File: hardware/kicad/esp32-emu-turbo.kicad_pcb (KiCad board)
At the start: 4 copper layers, 160 x 75 mm, 89 parts, among them J1 USB-C-16P, J3 JST-PH-2P-SMD, J4 FPC-40P-0.5mm, SW1 SW-SMD-5.1x5.1, SW10 SW-SMD-5.1x5.1, SW11 SW-SMD-5.1x5.1, SW12 SW-SMD-5.1x5.1, SW13 SW-SMD-5.1x5.1, SW2 SW-SMD-5.1x5.1, SW3 SW-SMD-5.1x5.1, SW4 SW-SMD-5.1x5.1, SW5 SW-SMD-5.1x5.1, SW6 SW-SMD-5.1x5.1, SW7 SW-SMD-5.1x5.1, SW8 SW-SMD-5.1x5.1, SW9 SW-SMD-5.1x5.1, U1 ESP32-S3-WROOM-1-N16R8, U2 ESOP-8, U3 SOT-223, U4 SOT-23-6, U5 SOP-16, U6 TF-01A

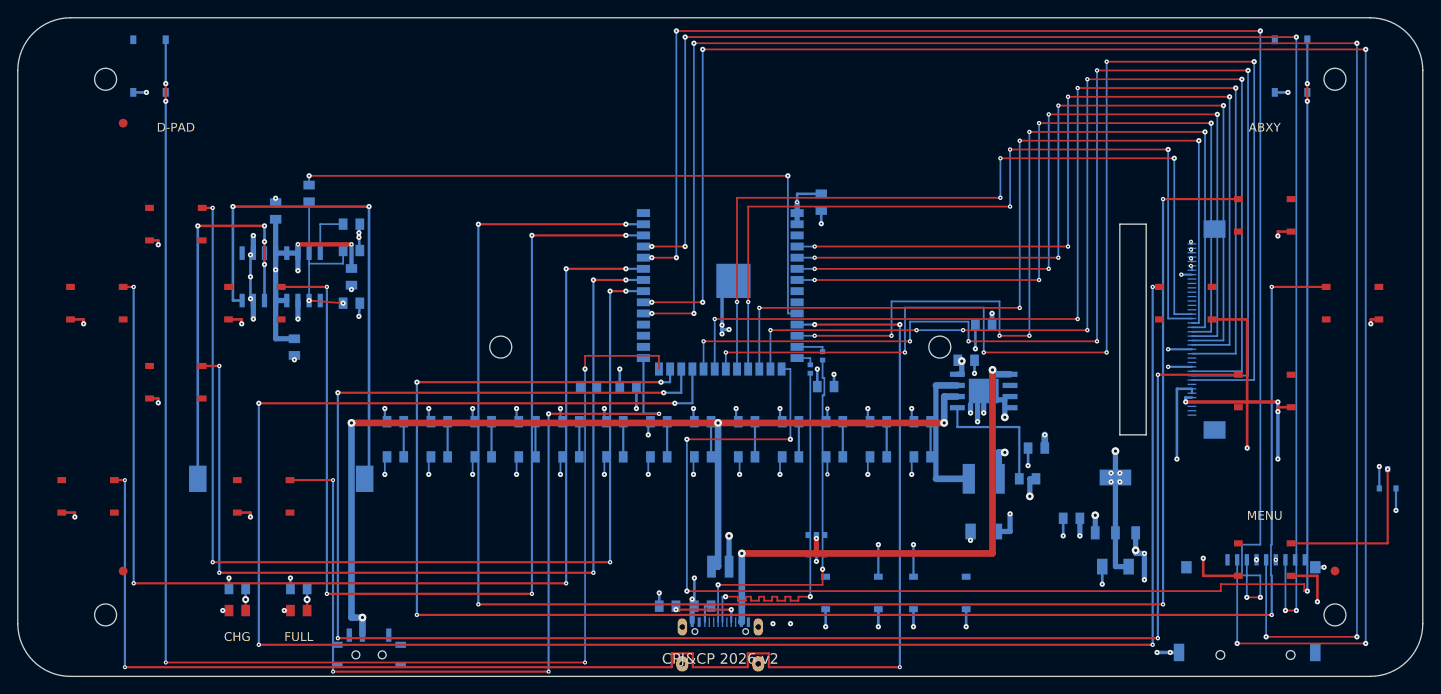
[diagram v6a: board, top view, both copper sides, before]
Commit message: fix(dfm): resolve 4 trace/via clearance violations + fix via-to-SMD false positive
- BTN_L approach column: shift x=64.60→64.75 (R8/C9 pad gap 0.05→0.20mm)
- BTN_UP approach column: add post-allocation pad clearance enforcement
  with oscillation-aware iteration (escapes R9/C10 pad cluster)
- BAT+ via: shift x=79.95→80.02 (R11 ring-to-pad gap 0.05→0.12mm)
- verify_dfm_v2.py: fix via-to-SMD test — use rectangular pad proximity
  instead of circumscribed circle (was inflating 1.0x1.3mm pad to r=0.82mm)
- New skill: /pcb-to-firmware (auto-propagate PCB changes to firmware)
- Updated PCBA renders (11 views, 1920x1080 raytraced)

Results: 115 DFM passed, 0 failed | 9 DFA passed | 358 design intent passed

Co-Authored-By: Claude Opus 4.6 (1M context) <noreply@anthropic.com>
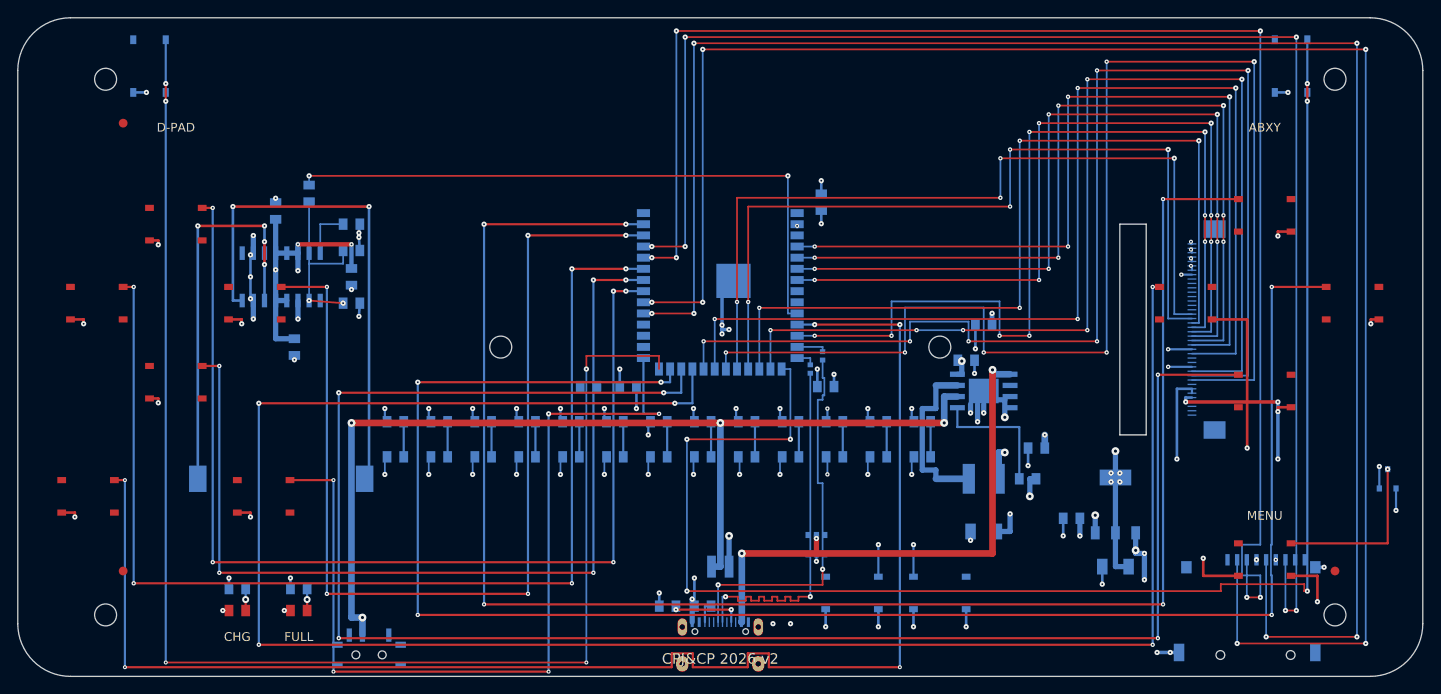
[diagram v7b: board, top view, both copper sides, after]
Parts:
- removed the C3 at (69.5, 42.0)
- removed the C4 at (92.0, 42.0)
- removed the C6 at (48.0, 50.0)
- removed the J1 at (80.0, 71.2)
- removed the J3 at (80.0, 62.5)
- removed the L1 at (110.0, 52.5)
- removed the R13 at (88.0, 46.0)
- removed the R14 at (93.0, 46.0)
- removed the R15 at (98.0, 46.0)
- removed the R16 at (115.0, 52.5)
- removed the R17 at (25.0, 65.0)
- removed the R18 at (32.0, 65.0)
- removed the R19 at (103.0, 46.0)
- removed the R22 at (90.2, 40.0)
- removed the R23 at (91.7, 38.5)
- removed the R3 at (65.0, 42.0)
- removed the R4 at (43.0, 46.0)
- removed the R5 at (48.0, 46.0)
- removed the R6 at (53.0, 46.0)
- removed the R7 at (58.0, 46.0)
- removed the R8 at (63.0, 46.0)
- removed the R9 at (68.0, 46.0)
- removed the SW5 at (142.0, 22.5)
- removed the SW6 at (152.0, 32.5)
- removed the SW7 at (142.0, 42.5)
- removed the U2 at (110.0, 42.5)
- removed the U4 at (91.0, 60.0)
- removed the U5 at (30.0, 29.5)
- added C1: C_0805, C_0805, B.Cu at (120.0, 57.0)
- added C10: C_0805, C_0805, B.Cu at (68.0, 50.0)
- added C11: C_0805, C_0805, B.Cu at (73.0, 50.0)
- added C12: C_0805, C_0805, B.Cu at (78.0, 50.0)
- added C13: C_0805, C_0805, B.Cu at (83.0, 50.0)
- added C14: C_0805, C_0805, B.Cu at (88.0, 50.0)
- added C15: C_0805, C_0805, B.Cu at (93.0, 50.0)
- added C16: C_0805, C_0805, B.Cu at (98.0, 50.0)
- added C17: C_0805, C_0805, B.Cu at (110.0, 35.0)
- added C18: C_0805, C_0805, B.Cu at (116.0, 49.0)
- added C19: C_1206, C_1206, B.Cu at (110.0, 58.5)
- added C2: C_1206, C_1206, B.Cu at (125.0, 62.5)
- added C20: C_0805, C_0805, B.Cu at (103.0, 50.0)
- added C21: C_0805, C_0805, B.Cu at (38.0, 23.5)
- added C22: C_0805, C_0805, B.Cu at (33.2, 20.0)
- added C23: C_0805, C_0805, B.Cu at (38.0, 29.5)
- added C24: C_0805, C_0805, B.Cu at (29.4, 22.0)
- added C25: C_0805, C_0805, B.Cu at (31.5, 37.5)
- added C27: C_0805, C_0805, B.Cu at (108.0, 39.0)
- added C8: C_0805, C_0805, B.Cu at (58.0, 50.0)
- added C9: C_0805, C_0805, B.Cu at (63.0, 50.0)
- added FID3: Fiducial, Fiducial, F.Cu at (12.0, 63.0)
- added R20: R_0805, R_0805, B.Cu at (38.0, 26.5)
- added R21: R_0805, R_0805, B.Cu at (38.0, 32.5)
- added SW11: SW-SMD-5.1x5.1, SW-SMD-5.1x5.1, B.Cu at (15.0, 5.50)
- added SW_RST: SW-SMD-5.1x5.1, SW-SMD-5.1x5.1, B.Cu at (95.0, 65.5)
- added U1: ESP32-S3-WROOM-1-N16R8, ESP32-S3-WROOM-1-N16R8, B.Cu at (80.0, 27.5)
- added U6: TF-01A, TF-01A, B.Cu at (140.0, 67.0)
- C6: renamed from FID3; value Fiducial -> C_0805; footprint Fiducial -> C_0805; moved to B.Cu
- J1: renamed from SW_RST; value SW-SMD-5.1x5.1 -> USB-C-16P; footprint SW-SMD-5.1x5.1 -> USB-C-16P
- J3: renamed from R12; value R_0805 -> JST-PH-2P-SMD; footprint R_0805 -> JST-PH-2P-SMD
- L1: renamed from R11; value R_0805 -> SMD-4x4x2; footprint R_0805 -> SMD-4x4x2
- R12: renamed from C21; value C_0805 -> R_0805; footprint C_0805 -> R_0805
- R13: renamed from C23; value C_0805 -> R_0805; footprint C_0805 -> R_0805
- R14: renamed from C24; value C_0805 -> R_0805; footprint C_0805 -> R_0805
- R15: renamed from C25; value C_0805 -> R_0805; footprint C_0805 -> R_0805
- R16: renamed from C2; value C_1206 -> R_0805; footprint C_1206 -> R_0805
- R17: renamed from C15; value C_0805 -> R_0805; footprint C_0805 -> R_0805
- R18: renamed from C16; value C_0805 -> R_0805; footprint C_0805 -> R_0805
- R19: renamed from C1; value C_0805 -> R_0805; footprint C_0805 -> R_0805
- R22: renamed from C9; value C_0805 -> R_0402; footprint C_0805 -> R_0402
- R23: renamed from C10; value C_0805 -> R_0402; footprint C_0805 -> R_0402
- R3: renamed from C11; value C_0805 -> R_0805; footprint C_0805 -> R_0805
- R4: renamed from C20; value C_0805 -> R_0805; footprint C_0805 -> R_0805
- R5: renamed from C17; value C_0805 -> R_0805; footprint C_0805 -> R_0805
- R6: renamed from C18; value C_0805 -> R_0805; footprint C_0805 -> R_0805
- R7: renamed from C19; value C_1206 -> R_0805; footprint C_1206 -> R_0805
- R8: renamed from C27; value C_0805 -> R_0805; footprint C_0805 -> R_0805
- R9: renamed from C22; value C_0805 -> R_0805; footprint C_0805 -> R_0805
- SW12: renamed from U6; value TF-01A -> SW-SMD-5.1x5.1; footprint TF-01A -> SW-SMD-5.1x5.1
- SW5: renamed from U1; value ESP32-S3-WROOM-1-N16R8 -> SW-SMD-5.1x5.1; footprint ESP32-S3-WROOM-1-N16R8 -> SW-SMD-5.1x5.1; moved to F.Cu
- SW6: renamed from SW11; moved to F.Cu
- SW7: renamed from SW12; moved to F.Cu
- U2: renamed from C26; value C_0805 -> ESOP-8; footprint C_0805 -> ESOP-8
- U4: renamed from C8; value C_0805 -> SOT-23-6; footprint C_0805 -> SOT-23-6
- U5: renamed from R10; value R_0805 -> SOP-16; footprint R_0805 -> SOP-16
- moved SW6 139.6 mm to (152.0, 32.5)
- moved R17 69.6 mm to (25.0, 65.0)
- moved R14 68.0 mm to (93.0, 46.0)
- moved R18 67.7 mm to (32.0, 65.0)
- moved R15 67.0 mm to (98.0, 46.0)
- moved R6 63.1 mm to (53.0, 46.0)
- moved R5 63.0 mm to (48.0, 46.0)
- moved SW5 62.2 mm to (142.0, 22.5)
- moved SW12 61.7 mm to (145.0, 5.50)
- moved R4 60.1 mm to (43.0, 46.0)
- moved R7 53.5 mm to (58.0, 46.0)
- moved R13 52.7 mm to (88.0, 46.0)
- moved R12 50.3 mm to (83.0, 46.0)
- moved U5 46.1 mm to (30.0, 29.5)
- moved R8 45.5 mm to (63.0, 46.0)
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- renumbered C14 to C26, C12 to C3, C13 to C4, R20 to R10, R21 to R11
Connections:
- C26 pad 1: (no net) -> +3V3
- C26 pad 2: (no net) -> GND
- C3 pad 1: (no net) -> +3V3
- C3 pad 2: (no net) -> GND
- C4 pad 1: (no net) -> +3V3
- C4 pad 2: (no net) -> GND
- C5 pad 1: (no net) -> BTN_UP
- C5 pad 2: (no net) -> GND
- C6 pad 1: (no net) -> BTN_DOWN
- C7 pad 1: (no net) -> BTN_LEFT
- C7 pad 2: (no net) -> GND
- J1 pad 1: EN -> GND
- J1 pad 2: (no net) -> VBUS
- J1 pad 3: GND -> (no net)
- J1 pad 4: GND -> USB_CC1
- J3 pad 1: (no net) -> BAT+
- J3 pad 2: (no net) -> GND
- J4 pad 37: (no net) -> GND
- L1 pad 1: (no net) -> BAT+
- L1 pad 2: (no net) -> LX
- R10 pad 1: GND -> BTN_X
- R10 pad 2: I2S_DOUT -> +3V3
- R11 pad 1: GND -> BTN_Y
- R11 pad 2: I2S_DOUT -> +3V3
- R12 pad 1: GND -> BTN_START
- R12 pad 2: PAM_VREF -> +3V3
- R13 pad 1: +5V -> BTN_SELECT
- R13 pad 2: GND -> +3V3
- R14 pad 1: GND -> BTN_L
- R14 pad 2: +5V -> +3V3
- R15 pad 1: +5V -> BTN_R
- R15 pad 2: GND -> +3V3
- R16 pad 1: +3V3 -> +5V
- R16 pad 2: GND -> IP5306_KEY
- R17 pad 1: (no net) -> LED1_RA
- R17 pad 2: (no net) -> +3V3
- R18 pad 1: (no net) -> LED2_RA
- R18 pad 2: (no net) -> +3V3
- R19 pad 1: +5V -> BTN_MENU
- R19 pad 2: GND -> +3V3
- R22 pad 1: (no net) -> USB_DP_MCU
- R22 pad 2: (no net) -> USB_D+
- R23 pad 1: (no net) -> USB_DM_MCU
- R23 pad 2: (no net) -> USB_D-
- R3 pad 1: (no net) -> BTN_DOWN
- R4 pad 1: (no net) -> BTN_UP
- R4 pad 2: (no net) -> +3V3
- R5 pad 1: VBUS -> BTN_DOWN
- R5 pad 2: GND -> +3V3
- R6 pad 1: BAT+ -> BTN_LEFT
- R6 pad 2: GND -> +3V3
- R7 pad 1: +5V -> BTN_RIGHT
- R7 pad 2: GND -> +3V3
- R8 pad 1: GND -> BTN_A
- R8 pad 2: +5V -> +3V3
- R9 pad 1: I2S_DOUT -> BTN_B
- R9 pad 2: I2S_DOUT -> +3V3
- SW12 pad 2: SD_CS -> GND
- SW12 pad 3: SD_MOSI -> BTN_R
- SW12 pad 4: +3V3 -> (no net)
- SW5 pad 1: (no net) -> BTN_A
- SW5 pad 2: +3V3 -> (no net)
- SW5 pad 4: LCD_D0 -> GND
- SW6 pad 1: (no net) -> BTN_B
- SW6 pad 2: GND -> (no net)
- SW6 pad 3: BTN_L -> (no net)
- SW6 pad 4: (no net) -> GND
- SW7 pad 1: (no net) -> BTN_X
- SW7 pad 2: GND -> (no net)
- SW7 pad 3: BTN_R -> (no net)
- SW7 pad 4: (no net) -> GND
- SW_PWR pad 4b: (no net) -> BTN_SELECT
- SW_PWR pad 4d: (no net) -> BTN_SELECT
- U2 pad 1: +3V3 -> VBUS
- U2 pad 2: GND -> (no net)
- U3 pad 2: (no net) -> +3V3
- U4 pad 1: (no net) -> USB_D-
- U4 pad 2: (no net) -> GND
- U5 pad 2: (no net) -> GND
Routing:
- net +3V3: track 62.6 -> 58.1 mm, vias 26 -> 27
- net LX: track 16.8 -> 19.9 mm
- net BTN_A: track 198.8 -> 197.5 mm
- net USB_D-: track 42.1 -> 43.2 mm
- net LCD_D4: vias 6 -> 8
- net LCD_D3: vias 4 -> 6
- net LCD_D2: vias 4 -> 6
- net LCD_D1: vias 4 -> 6

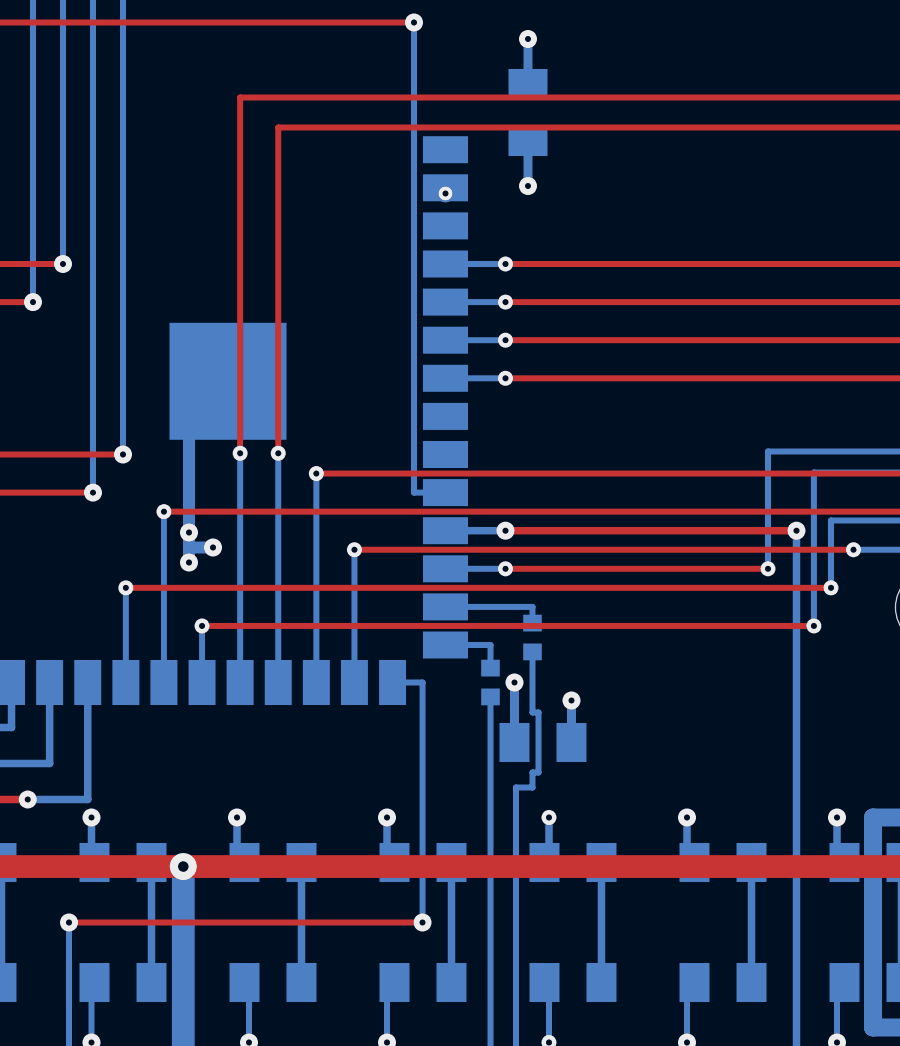
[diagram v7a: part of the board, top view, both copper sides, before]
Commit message: fix(critical): GPIO45 VDD_SPI strapping + 13 DRC shorts + C28 bulk cap
CRITICAL: GPIO45 (BTN_L) had external 10k pull-up forcing VDD_SPI=1.8V
at boot — Octal PSRAM requires 3.3V and would not function. Fix: skip
R14 pull-up in routing (i=10 continue), firmware uses internal pull-up.

PCB routing fixes (13→0 real shorts):
- 52 pad-net assignments added (R4-R15,R19, C5-C16,C20 in _init_pads)
- Approach column forbidden zones (pull-up/debounce pads + C3 + R3)
- USB_D- jog x=91.10 around R14 pad
- LX jog x=103.00 between R19 pads
- BAT+ shift 79.75→80.01 (clears R11 + J3)
- +3V3 via moved above pin 2 (avoids GND thermal pad)
- J4:42 F.Cu bridge for 4 LCD data traces
- 9 explicit pad-net assignments (U2,U3,SW_PWR,U6,J4,R3)
- C26 routing: own via instead of old +3V3 via

New component:
- C28 (10uF 0805) at (86,26): ESP32 +3V3 bulk cap, 3.7mm from pin 2

Firmware: board_config.h updated with BTN_L internal pull-up note

DFM: 115/115 | DFA: 9/9 | DRC: 0 real shorts | Datasheet: 259/259

Co-Authored-By: Claude Opus 4.6 (1M context) <noreply@anthropic.com>
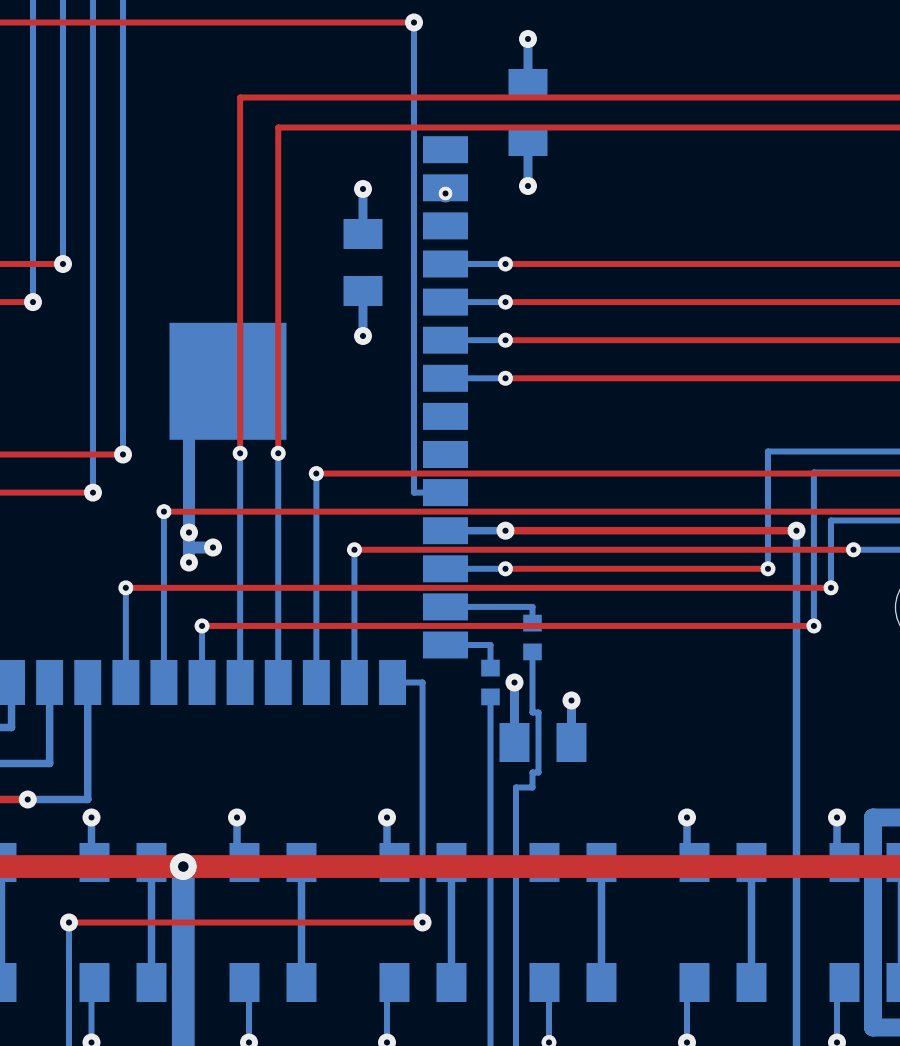
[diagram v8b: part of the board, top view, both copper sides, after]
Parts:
- removed the C24 at (29.4, 22.0)
- removed the L1 at (110.0, 52.5)
- removed the SW10 at (28.0, 54.5)
- added C28: C_0805, C_0805, B.Cu at (86.0, 26.0)
- added FID1: Fiducial, Fiducial, F.Cu at (12.0, 12.0)
- added LED1: LED_0805, LED_0805, F.Cu at (25.0, 67.5)
- added SW_RST: SW-SMD-5.1x5.1, SW-SMD-5.1x5.1, B.Cu at (95.0, 65.5)
- C24: renamed from FID1; value Fiducial -> C_0805; footprint Fiducial -> C_0805; moved to B.Cu
- L1: renamed from SW_RST; value SW-SMD-5.1x5.1 -> SMD-4x4x2; footprint SW-SMD-5.1x5.1 -> SMD-4x4x2
- SW10: renamed from LED1; value LED_0805 -> SW-SMD-5.1x5.1; footprint LED_0805 -> SW-SMD-5.1x5.1
- moved C24 20.0 mm to (29.4, 22.0)
- moved L1 19.8 mm to (110.0, 52.5)
- moved SW10 13.3 mm to (28.0, 54.5)
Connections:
- C24 pad 1: (no net) -> GND
- L1 pad 1: EN -> BAT+
- L1 pad 2: (no net) -> LX
- R14 pad 2: +3V3 -> (no net)
- SW10 pad 1: GND -> (no net)
- SW10 pad 2: LED1_RA -> BTN_SELECT
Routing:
- net GND: track 183.4 -> 184.9 mm, vias 82 -> 83
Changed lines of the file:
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@@
     (property "Value" "R_0805" (at 0 3 0) (layer "B.Fab") (effects (font (size 0.6 0.6) (thickness 0.2)) (justify mirror)))
     (pad "1" smd rect (at 0.95 0) (size 1.0 1.3) (layers "B.Cu" "B.Paste" "B.Mask") (net 37 "BTN_L"))
-    (pad "2" smd rect (at -0.95 0) (size 1.0 1.3) (layers "B.Cu" "B.Paste" "B.Mask") (net 4 "+3V3"))
+    (pad "2" smd rect (at -0.95 0) (size 1.0 1.3) (layers "B.Cu" "B.Paste" "B.Mask") (net 0 ""))
   )
   (footprint "R_0805" (at 98 46) (layer "B.Cu")
@@
     (pad "1" smd rect (at 0.95 0) (size 1.0 1.3) (layers "B.Cu" "B.Paste" "B.Mask") (net 1 "GND"))
     (pad "2" smd rect (at -0.95 0) (size 1.0 1.3) (layers "B.Cu" "B.Paste" "B.Mask") (net 3 "+5V"))
+  )
+  (footprint "C_0805" (at 86.0 26.0) (layer "B.Cu")
+    (property "Reference" "C28" (at 0 -3 0) (layer "B.Fab") (effects (font (size 0.6 0.6) (thickness 0.2)) (justify mirror)))
+    (property "Value" "C_0805" (at 0 3 0) (layer "B.Fab") (effects (font (size 0.6 0.6) (thickness 0.2)) (justify mirror)))
+    (pad "1" smd rect (at 0.0 -0.95) (size 1.3 1.0) (layers "B.Cu" "B.Paste" "B.Mask") (net 4 "+3V3"))
+    (pad "2" smd rect (at 0.0 0.95) (size 1.3 1.0) (layers "B.Cu" "B.Paste" "B.Mask") (net 1 "GND"))
   )
   (footprint "C_0805" (at 33.175 20.0) (layer "B.Cu")
@@
   (segment (start 86.8 46) (end 86.8 44.5) (width 0.25) (layer "B.Cu") (net 4))
   (via (at 86.8 44.5) (size 0.6) (drill 0.2) (layers "F.Cu" "B.Cu") (net 4))
-  (segment (start 92.05 46) (end 92.2 46) (width 0.25) (layer "B.Cu") (net 4))
-  (segment (start 92.2 46) (end 92.2 44.5) (width 0.25) (layer "B.Cu") (net 4))
-  (via (at 92.2 44.5) (size 0.5) (drill 0.2) (layers "F.Cu" "B.Cu") (net 4))
   (segment (start 97.05 46) (end 96.8 46) (width 0.25) (layer "B.Cu") (net 4))
   (segment (start 96.8 46) (end 96.8 44.5) (width 0.25) (layer "B.Cu") (net 4))
@@
   (segment (start 91.5 21.95) (end 91.5 23.45) (width 0.3) (layer "B.Cu") (net 1))
   (via (at 91.5 23.45) (size 0.6) (drill 0.2) (layers "F.Cu" "B.Cu") (net 1))
+  (segment (start 86.0 25.05) (end 86.0 23.55) (width 0.3) (layer "B.Cu") (net 4))
+  (via (at 86.0 23.55) (size 0.6) (drill 0.2) (layers "F.Cu" "B.Cu") (net 4))
+  (segment (start 86.0 26.95) (end 86.0 28.45) (width 0.3) (layer "B.Cu") (net 1))
+  (via (at 86.0 28.45) (size 0.6) (drill 0.2) (layers "F.Cu" "B.Cu") (net 1))
   (segment (start 120.95 57.0) (end 120.95 59.0) (width 0.6) (layer "B.Cu") (net 3))
   (via (at 120.95 59.0) (size 0.6) (drill 0.2) (layers "F.Cu" "B.Cu") (net 3))
